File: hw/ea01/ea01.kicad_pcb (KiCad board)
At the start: 2 copper layers, 100 x 45 mm, 189 parts, among them J1 Screw_Terminal_01x02, J10 Screw_Terminal_01x02, J11 Screw_Terminal_01x02, J13 Conn_01x02_Pin, J14 Conn_01x02_Pin, J15 Conn_01x02_Pin, J16 Conn_01x02_Pin, J17 Conn_01x02_Pin, J18 Conn_01x02_Pin, J19 Conn_01x02_Pin, J2 USB_B, J3 Conn_01x05_Pin, J4 Screw_Terminal_01x02, J5 Screw_Terminal_01x02, J6 Screw_Terminal_01x03, J7 Conn_01x03_Pin, J8 Conn_01x03_Pin, K1 G5NB, K2 G5NB, Q11 BC817, Q2 BC817, Q3 BC817, Q4 BC817, Q5 BC817, Q6 BC817, Q7 BC817, Q9 BC817, SW1 SW_Push, SW2 SW_Push, SW3 SW_Push, SW4 SW_Push, U1 RP2040, U11 W25Q32JVSS, U12 SN75176AP, U13 PC817, U14 PC817, U2 PCF8563T, U3 74HC14, U4 MC34063AD, U5 MCP9700Ax-ELT, U6 AMS1117-3.3, U8 CAT24C256, Y1 12Mhz, Y3 32.768Khz

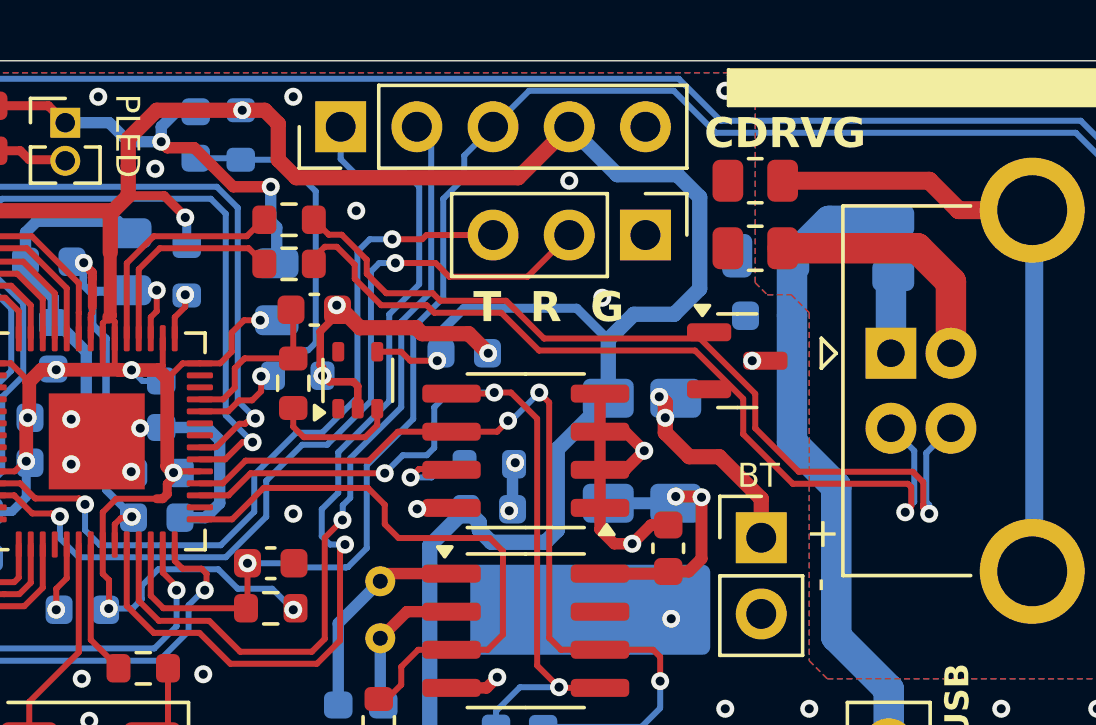
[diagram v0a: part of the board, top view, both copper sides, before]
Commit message: 3d models updated
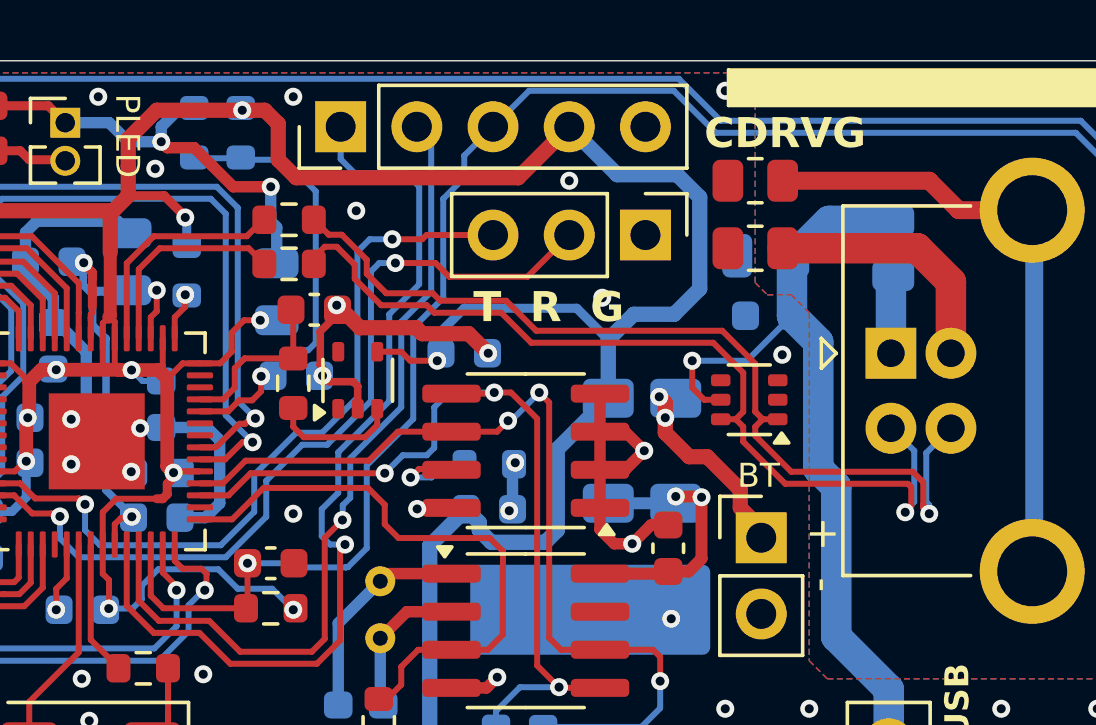
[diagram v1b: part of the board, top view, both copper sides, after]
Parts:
- removed D1: NUP2105L, Package_TO_SOT_SMD:SOT-23
- added U7: NUP2202, Package_TO_SOT_SMD:SOT-363_SC-70-6, F.Cu at (151.2, 60.3)
- moved R82 8.80 mm to (132.7, 51.4), turned to 90 degrees
- moved C63 8.70 mm to (136.1, 59.5), turned to 0 degrees
- moved R81 0.08 mm to (134.2, 51.4)
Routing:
- net VBUS: track 21.5 -> 27.5 mm, vias 0 -> 1
- net /mcu/UDB_D+: track 29.7 -> 31.1 mm
- net /mcu/USB_D-: track 28.9 -> 30.3 mm
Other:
- board text added: "1 0 Vb0"
- board text added: "1 0 Vb1"
- board text added: "ADDR"
